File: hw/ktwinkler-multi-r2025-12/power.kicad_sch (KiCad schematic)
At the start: 11 parts, among them J1 USB_C_Receptacle_USB2.0_16P, J4 Conn_01x02, U1 TPS631000DRLR, U7 SRV05-4

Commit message: ktwinkler hw dev: progress stash
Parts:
- removed C1: 22uF, Capacitor_SMD:C_0603_1608Metric, symbol Device:C_Small
- added C1, C15, C16: 22uF, Capacitor_SMD:C_0805_2012Metric, symbol karl-atomic-basic:KC0805_22uF_25V
- added J2: Conn_01x02, Connector_PinHeader_2.54mm:PinHeader_1x02_P2.54mm_Vertical, symbol Connector_Generic:Conn_01x02
- added R6: 0R, Resistor_SMD:R_0402_1005Metric, symbol karl-atomic-basic:KR0402_0R
- added R7: 39k, Resistor_SMD:R_0402_1005Metric, symbol karl-atomic-basic:KR0402_39k
- added R8: 220k, Resistor_SMD:R_0402_1005Metric, symbol karl-atomic-basic:KR0402_220k
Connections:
- net +BATT: now also U1.4 (VIN), U1.5 (EN), C16.1, J2.2 (Pin_2)
- net GND: now also U1.7 (GND), C1.2, C15.2, C16.2, J2.1 (Pin_1), R6.1, R7.2
- net +3V3: now reaches U1.1 (VOUT)
- net +3V3: now also C1.1, C15.1, R8.1
- net at U1.6 (MODE): now also R6.2
- net at U1.8 (FB): now also R7.1, R8.2
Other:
- note added: "Low R2 must not exceed 100k And we want to use 0402, for "reasons" which has much more limited selection at jlc basic hi R1 = low R2 x ((3.3/0.5)-1) => 68k/380k nominal (TI use 91k for everything, but that's not in basic in 0402) 68k/330k => 2.9V 68k/470k => 3.95V Both those are bad... 51k/330k => 3.7 56k/330k => 3.44? 39k/220k => 3.32? best we can do 33k/220k => (r1/r2 +1) * 0.5 => vout"
- note added: "Remember, this is _only_ the power supply for the esp32 or ch5xx, it doesn't need to power the leds!"
- note added: "TI promises a single 0805 output, 47uf! not sure...."
- moved on the sheet: J4, L1, U1

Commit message: pushing onwards like a madlad
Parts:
- removed C3, C4: 100nF, Capacitor_SMD:C_0603_1608Metric, symbol karl-atomic-basic:KC0603_100nF
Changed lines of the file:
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@@
-	)
-	(symbol
-		(lib_id "karl-atomic-basic:KC0603_100nF")
-		(at 148.59 116.84 0)
-		(unit 1)
-		(exclude_from_sim no)
-		(in_bom yes)
-		(on_board yes)
-		(dnp no)
-		(fields_autoplaced yes)
-		(property "Reference" "C3"
-			(at 151.13 115.0671 0)
-			(effects
-				(font
-					(size 1.27 1.27)
-				)
-				(justify left)
-			)
-		)
-		(property "Value" "100nF"
-			(at 151.13 117.6071 0)
-			(effects
-				(font
-					(size 1.27 1.27)
-				)
-				(justify left)
-			)
-		)
-		(property "Footprint" "Capacitor_SMD:C_0603_1608Metric"
-			(at 148.082 120.65 0)
-			(effects
-				(font
-					(size 1.27 1.27)
-				)
-				(hide yes)
-			)
-		)
-		(property "Datasheet" "~"
-			(at 148.59 116.84 0)
-			(effects
-				(font
-					(size 1.27 1.27)
-				)
-				(hide yes)
-			)
-		)
-		(property "Description" "50V, X7R"
-			(at 148.59 120.65 0)
-			(effects
-				(font
-					(size 1.27 1.27)
-				)
-				(hide yes)
-			)
-		)
-		(property "MPN" "CC0603KRX7R9BB104"
-			(at 148.336 120.65 0)
-			(effects
-				(font
-					(size 1.27 1.27)
-				)
-				(hide yes)
-			)
-		)
-		(property "LCSC Part #" "C14663"
-			(at 148.59 120.65 0)
-			(effects
-				(font
-					(size 1.27 1.27)
-				)
-				(hide yes)
-			)
-		)
-		(pin "2"
-		)
-		(pin "1"
-		)
-		(instances
-			(project "ktwinkler-multi-r2025-12"
-				(path "/48773b41-b773-40e2-8ba4-2e78c7a3e45f/974aa20f-6384-4103-a4af-e95b95e9bb34"
-					(reference "C3")
-					(unit 1)
-				)
-			)
-		)
-	)
-	(symbol
-		(lib_id "karl-atomic-basic:KC0603_100nF")
-		(at 160.02 116.84 0)
-		(unit 1)
-		(exclude_from_sim no)
-		(in_bom yes)
-		(on_board yes)
-		(dnp no)
-		(fields_autoplaced yes)
-		(property "Reference" "C4"
-			(at 162.56 115.0671 0)
-			(effects
-				(font
-					(size 1.27 1.27)
-				)
-				(justify left)
-			)
-		)
-		(property "Value" "100nF"
-			(at 162.56 117.6071 0)
-			(effects
-				(font
-					(size 1.27 1.27)
-				)
-				(justify left)
-			)
-		)
-		(property "Footprint" "Capacitor_SMD:C_0603_1608Metric"
-			(at 159.512 120.65 0)
-			(effects
-				(font
-					(size 1.27 1.27)
-				)
-				(hide yes)
-			)
-		)
-		(property "Datasheet" "~"
-			(at 160.02 116.84 0)
-			(effects
-				(font
-					(size 1.27 1.27)
-				)
-				(hide yes)
-			)
-		)
-		(property "Description" "50V, X7R"
-			(at 160.02 120.65 0)
-			(effects
-				(font
-					(size 1.27 1.27)
-				)
-				(hide yes)
-			)
-		)
-		(property "MPN" "CC0603KRX7R9BB104"
-			(at 159.766 120.65 0)
-			(effects
-				(font
-					(size 1.27 1.27)
-				)
-				(hide yes)
-			)
-		)
-		(property "LCSC Part #" "C14663"
-			(at 160.02 120.65 0)
-			(effects
-				(font
-					(size 1.27 1.27)
-				)
-				(hide yes)
-			)
-		)
-		(pin "2"
-		)
-		(pin "1"
-		)
-		(instances
-			(project "ktwinkler-multi-r2025-12"
-				(path "/48773b41-b773-40e2-8ba4-2e78c7a3e45f/974aa20f-6384-4103-a4af-e95b95e9bb34"
-					(reference "C4")
-					(unit 1)
-				)
-			)
-		)
 	)
 	(symbol
@@
 		(on_board yes)
 		(dnp no)
-		(fields_autoplaced yes)
 		(property "Reference" "R1"
-			(at 86.36 43.18 90)
+			(at 82.804 46.736 90)
 			(effects
 				(font
@@
 		)
 		(property "Value" "5k1"
-			(at 86.36 45.72 90)
+			(at 90.424 46.736 90)
 			(effects
 				(font
@@
 		(on_board yes)
 		(dnp no)
-		(fields_autoplaced yes)
 		(property "Reference" "R2"
-			(at 86.36 45.72 90)
+			(at 82.804 52.324 90)
 			(effects
 				(font
@@
 		)
 		(property "Value" "5k1"
-			(at 86.36 48.26 90)
-			(effects
-				(font
+			(at 90.17 52.324 90)
+			(effects
+				(font

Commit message: ready for scope creep
I think the schematic is ... mostly ok?  I need to decide how much of
the han p1 port scope creep to bother doing, or not...

I've roughyl blocked out the board, seems as good as any?
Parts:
- removed R6: 0R, Resistor_SMD:R_0402_1005Metric, symbol karl-atomic-basic:KR0402_0R
- removed U7: SRV05-4, Package_TO_SOT_SMD:SOT-23-6, symbol karl-atomic-basic:SRV05-4
- added R4, R5: 22R, Resistor_SMD:R_0402_1005Metric, symbol karl-atomic-basic:KR0402_22R
- added R6: 10k, Resistor_SMD:R_0402_1005Metric, symbol karl-atomic-basic:KR0402_10k
- added U6: Protection_H5VU25UC, Package_DFN_QFN:Diodes_UDFN-10_1.0x2.5mm_P0.5mm, symbol karl-atomic-basic:Protection_H5VU25UC
- C1, C15, C16: jlcbasic (none) -> basic
- J1: footprint Connector_USB:USB_C_Receptacle_GCT_USB4110 -> Connector_USB:USB_C_Receptacle_GCT_USB4105-xx-A_16P_TopMnt_Horizontal; LCSC Part # (none) -> C2988369; MPN (none) -> GT-USB-7010ASV
- J4: footprint Connector_Phoenix_MC:PhoenixContact_MCV_1,5_2-G-3.81_1x02_P3.81mm_Vertical -> Connector_Phoenix_MC:PhoenixContact_MC_1,5_2-G-3.5_1x02_P3.50mm_Horizontal; LCSC Part # C8396 -> C8387
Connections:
- net GND: now also R6.1, U6.3 (GND)
- net USBDM: now also R4.2; no longer J1.A7 (D-), J1.B7 (D-)
- net USBDP: now also R5.2; no longer J1.A6 (D+), J1.B6 (D+)
- net VBUS: now also U6.8 (VBUS)
- net at U1.6 (MODE): now also R6.2
- new net: U6.10 (NC), U6.6 (NC), U6.7 (NC), U6.9 (NC)
- new net DMinusIn: J1.A7 (D-), J1.B7 (D-), R4.1, U6.2 (I/O2)
- new net DPlusIn: J1.A6 (D+), J1.B6 (D+), R5.1, U6.4 (I/O3)
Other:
- note added: "eh, esp32 wants them, ch58x has them internal, just slap em down"

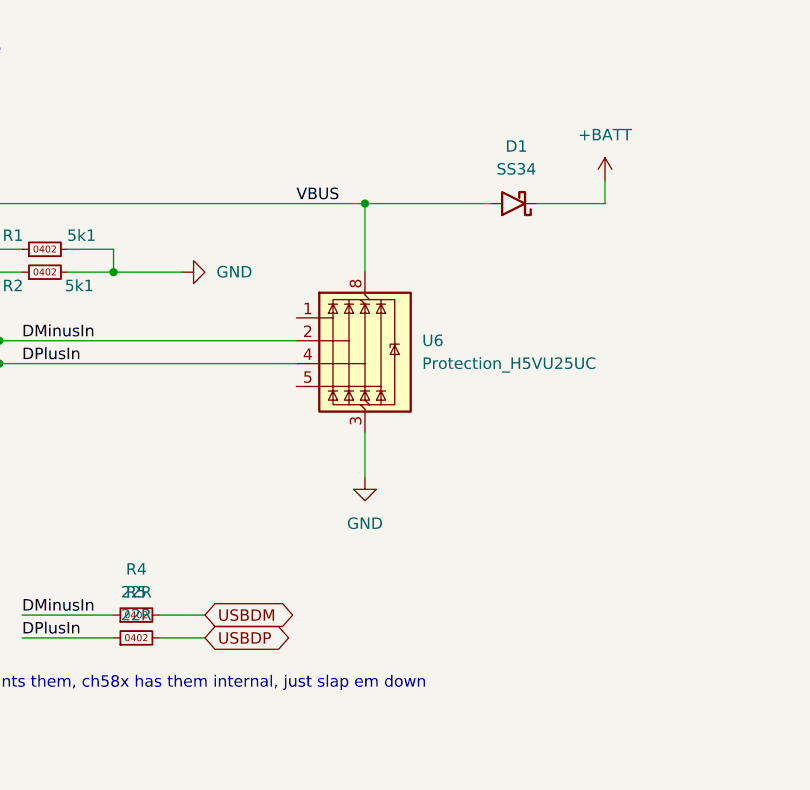
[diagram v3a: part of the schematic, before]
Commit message: update following ERC and symbol fixes
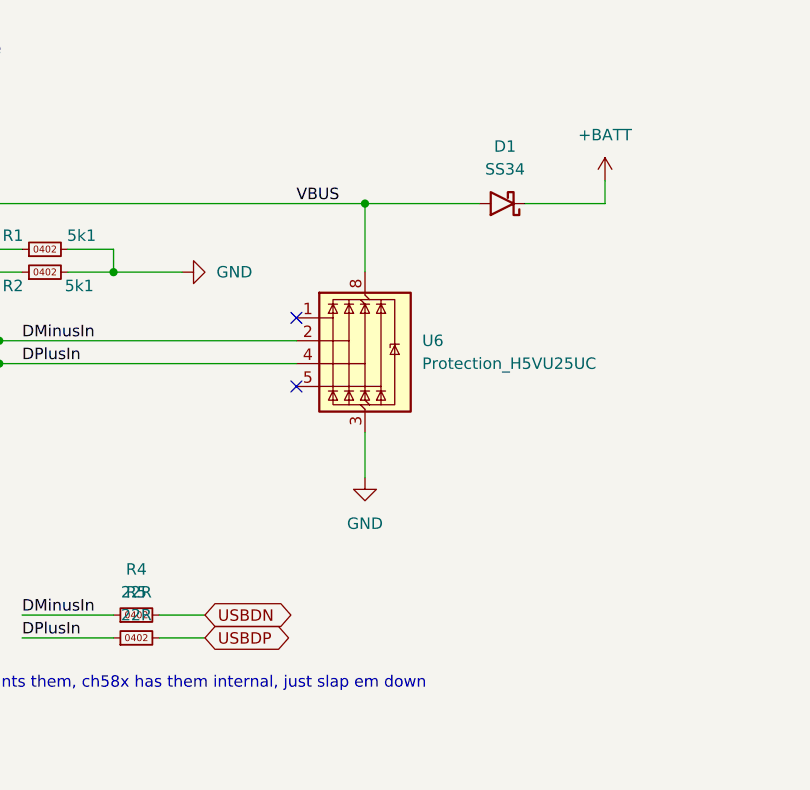
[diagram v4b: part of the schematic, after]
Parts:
- D1: symbol karl-atomic-basic:SS34 -> karl-atomic-basic:Diode_SS34
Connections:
- net USBDM renamed USBDN
- no-connect marks 2 -> 4
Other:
- moved on the sheet: D1
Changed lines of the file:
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@@
+	)
+	(junction
+		(at 53.34 83.82)
+		(diameter 0)
+		(color 0 0 0 0)
+	)
+	(junction
+		(at 58.42 152.4)
+		(diameter 0)
+		(color 0 0 0 0)
+	)
+	(junction
+		(at 121.92 43.18)
+		(diameter 0)
+		(color 0 0 0 0)
+	)
+	(junction
+		(at 154.94 152.4)
+		(diameter 0)
+		(color 0 0 0 0)
+	)
+	(junction
+		(at 144.78 162.56)
+		(diameter 0)
+		(color 0 0 0 0)
+	)
+	(junction
+		(at 81.28 58.42)
+		(diameter 0)
+		(color 0 0 0 0)
+	)
+	(junction
+		(at 144.78 152.4)
+		(diameter 0)
+		(color 0 0 0 0)
 	)
 	(junction
@@
 		(color 0 0 0 0)
 	)
-	(junction
-		(at 53.34 83.82)
-		(diameter 0)
-		(color 0 0 0 0)
-	)
-	(junction
-		(at 58.42 152.4)
-		(diameter 0)
-		(color 0 0 0 0)
-	)
-	(junction
-		(at 121.92 43.18)
-		(diameter 0)
-		(color 0 0 0 0)
-	)
-	(junction
-		(at 154.94 152.4)
-		(diameter 0)
-		(color 0 0 0 0)
-	)
-	(junction
-		(at 144.78 162.56)
-		(diameter 0)
-		(color 0 0 0 0)
-	)
-	(junction
-		(at 81.28 58.42)
-		(diameter 0)
-		(color 0 0 0 0)
-	)
-	(junction
-		(at 144.78 152.4)
-		(diameter 0)
-		(color 0 0 0 0)
-	)
 	(no_connect
 		(at 76.2 73.66)
@@
 		(at 76.2 71.12)
 	)
+	(no_connect
+		(at 114.3 55.88)
+	)
+	(no_connect
+		(at 114.3 63.5)
+	)
 	(wire
 		(pts
@@
 	(wire
 		(pts
+			(xy 119.38 160.02) (xy 129.54 160.02)
+		)
+		(stroke
+			(width 0)
+			(type default)
+		)
+	)
+	(wire
+		(pts
+			(xy 76.2 55.88) (xy 81.28 55.88)
+		)
+		(stroke
+			(width 0)
+			(type default)
+		)
+	)
+	(wire
+		(pts
+			(xy 58.42 152.4) (xy 58.42 149.86)
+		)
+		(stroke
+			(width 0)
+			(type default)
+		)
+	)
+	(wire
+		(pts
+			(xy 144.78 162.56) (xy 144.78 172.72)
+		)
+		(stroke
+			(width 0)
+			(type default)
+		)
+	)
+	(wire
+		(pts
+			(xy 129.54 152.4) (xy 129.54 154.94)
+		)
+		(stroke
+			(width 0)
+			(type default)
+		)
+	)
+	(wire
+		(pts
 			(xy 119.38 152.4) (xy 129.54 152.4)
 		)
@@
 	(wire
 		(pts
-			(xy 119.38 160.02) (xy 129.54 160.02)
-		)
-		(stroke
-			(width 0)
-			(type default)
-		)
-	)
-	(wire
-		(pts
-			(xy 76.2 55.88) (xy 81.28 55.88)
-		)
-		(stroke
-			(width 0)
-			(type default)
-		)
-	)
-	(wire
-		(pts
-			(xy 58.42 152.4) (xy 58.42 149.86)
-		)
-		(stroke
-			(width 0)
-			(type default)
-		)
-	)
-	(wire
-		(pts
-			(xy 144.78 162.56) (xy 144.78 172.72)
-		)
-		(stroke
-			(width 0)
-			(type default)
-		)
-	)
-	(wire
-		(pts
-			(xy 129.54 152.4) (xy 129.54 154.94)
-		)
-		(stroke
-			(width 0)
-			(type default)
-		)
-	)
-	(wire
-		(pts
 			(xy 93.98 48.26) (xy 93.98 50.8)
 		)
@@
 	(wire
 		(pts
-			(xy 121.92 43.18) (xy 135.89 43.18)
+			(xy 121.92 43.18) (xy 134.62 43.18)
 		)
 		(stroke
@@
 	(wire
 		(pts
-			(xy 140.97 43.18) (xy 148.59 43.18)
+			(xy 139.7 43.18) (xy 148.59 43.18)
 		)
 		(stroke
@@
 	(label "DMinusIn"
 		(at 83.82 58.42 0)
+		(fields_autoplaced yes)
 		(effects
 			(font
@@
 			(justify left bottom)
 		)
+		(property "Netclass" "usb-7628"
+			(at 83.82 59.69 0)
+			(effects
+				(font
+					(size 1.27 1.27)
+					(italic yes)
+				)
+				(justify left)
+			)
+		)
 	)
 	(label "DPlusIn"
 		(at 83.82 60.96 0)
+		(fields_autoplaced yes)
 		(effects
 			(font
@@
 			)
 			(justify left bottom)
+		)
+		(property "Netclass" "usb-7628"
+			(at 83.82 62.23 0)
+			(effects
+				(font
+					(size 1.27 1.27)
+					(italic yes)
+				)
+				(justify left)
+			)
 		)
 	)
@@
 		)
 	)
-	(global_label "USBDM"
+	(global_label "USBDN"
 		(shape bidirectional)
 		(at 104.14 88.9 0)
@@
 		)
 		(property "Intersheetrefs" "${INTERSHEET_REFS}"
-			(at 114.7679 88.9 0)
+			(at 114.647 88.9 0)
 			(effects
 				(font
@@
 	)
 	(symbol
-		(lib_id "karl-atomic-basic:SS34")
-		(at 138.43 43.18 180)
+		(lib_id "karl-atomic-basic:Diode_SS34")
+		(at 137.16 43.18 180)
 		(unit 1)
 		(exclude_from_sim no)
@@
 		(fields_autoplaced yes)
 		(property "Reference" "D1"
-			(at 138.7475 36.83 0)
+			(at 137.4775 36.83 0)
 			(effects
 				(font
@@
 		)
 		(property "Value" "SS34"
-			(at 138.7475 39.37 0)
+			(at 137.4775 39.37 0)
 			(effects
 				(font
@@
 		)
 		(property "Footprint" "Diode_SMD:D_SMA"
-			(at 138.43 38.735 0)
+			(at 137.16 38.735 0)
 			(effects
 				(font
@@
 		)
 		(property "Datasheet" "https://jlcpcb.com/api/file/downloadByFileSystemAccessId/8586172667489079296"
-			(at 138.43 43.18 0)
+			(at 137.16 43.18 0)
 			(effects
 				(font
@@
 		)
 		(property "Description" "40V 3A Schottky Barrier Rectifier Diode, SMA"
-			(at 138.43 43.18 0)
+			(at 137.16 43.18 0)
 			(effects
 				(font
@@
 		)
 		(property "LCSC Part #" "C8678"
-			(at 138.43 43.18 0)
+			(at 137.16 43.18 0)
 			(effects
 				(font
@@
 		)
 		(property "jlcbasic" "basic"
-			(at 138.43 43.18 0)
+			(at 137.16 43.18 0)
 			(effects
 				(font
@@
 		)
 		(property "MPN" "SS34"
-			(at 138.43 43.18 0)
-			(effects
-				(font
+			(at 137.16 43.18 0)
+			(effects
+				(font

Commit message: streammmm updates
"complete" apart from finishing those antennas.
needs DRC cleanups on both the wch inv-f and also the yolo-pole.
need to at least _basically_ get the antenna trace basic wdith correct
as well.  yolo is fine, when it's guided yolo, not "lol"
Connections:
- now unconnected: U6.10 (NC), U6.6 (NC), U6.7 (NC), U6.9 (NC)

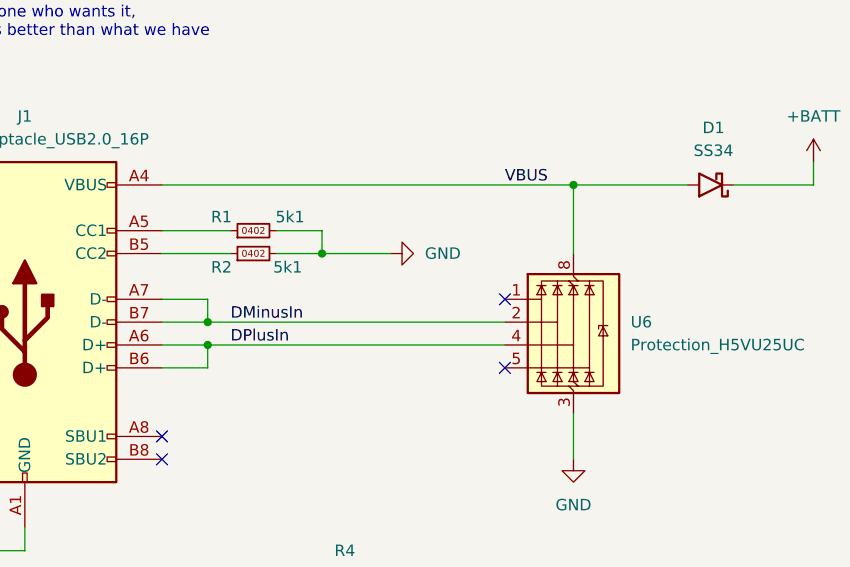
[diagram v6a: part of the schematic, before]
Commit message: hw/ktwinkler-multi: fix the bi/uni tvs fuckup
We're not likely to make a new version of _exactly_ this board, but
don't leave the totally busted short circuit around to stumble on later!
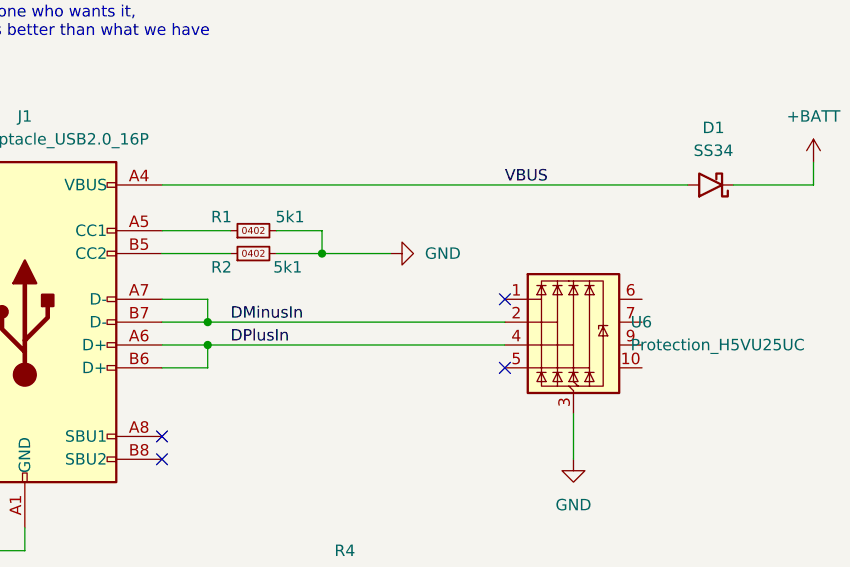
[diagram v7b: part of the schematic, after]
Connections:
- net GND: now also U6.8 (GND)
- net VBUS: no longer U6.8 (VBUS)
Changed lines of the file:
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@@
-	)
-	(junction
-		(at 121.92 43.18)
-		(diameter 0)
-		(color 0 0 0 0)
 	)
 	(junction
@@
 	(wire
 		(pts
-			(xy 121.92 43.18) (xy 121.92 50.8)
-		)
-		(stroke
-			(width 0)
-			(type default)
-		)
-	)
-	(wire
-		(pts
 			(xy 50.8 184.15) (xy 50.8 181.61)
 		)
@@
 	(wire
 		(pts
-			(xy 121.92 43.18) (xy 134.62 43.18)
-		)
-		(stroke
-			(width 0)
-			(type default)
-		)
-	)
-	(wire
-		(pts
-			(xy 76.2 43.18) (xy 121.92 43.18)
-		)
-		(stroke
+			(xy 76.2 43.18) (xy 134.62 43.18)
+		)
+		(stroke
